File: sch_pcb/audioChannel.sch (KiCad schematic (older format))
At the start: 87 parts, among them J201 TO_SOUNDCARD, J202 FROM_SOUNDCARD, J203 Radio Port, J404 DB9_FEMALE, Q201 2N7000, Q202 2N7000, Q203 2N7000, U103 MCP4351, U106 MCP4351, U201 MCP6004N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

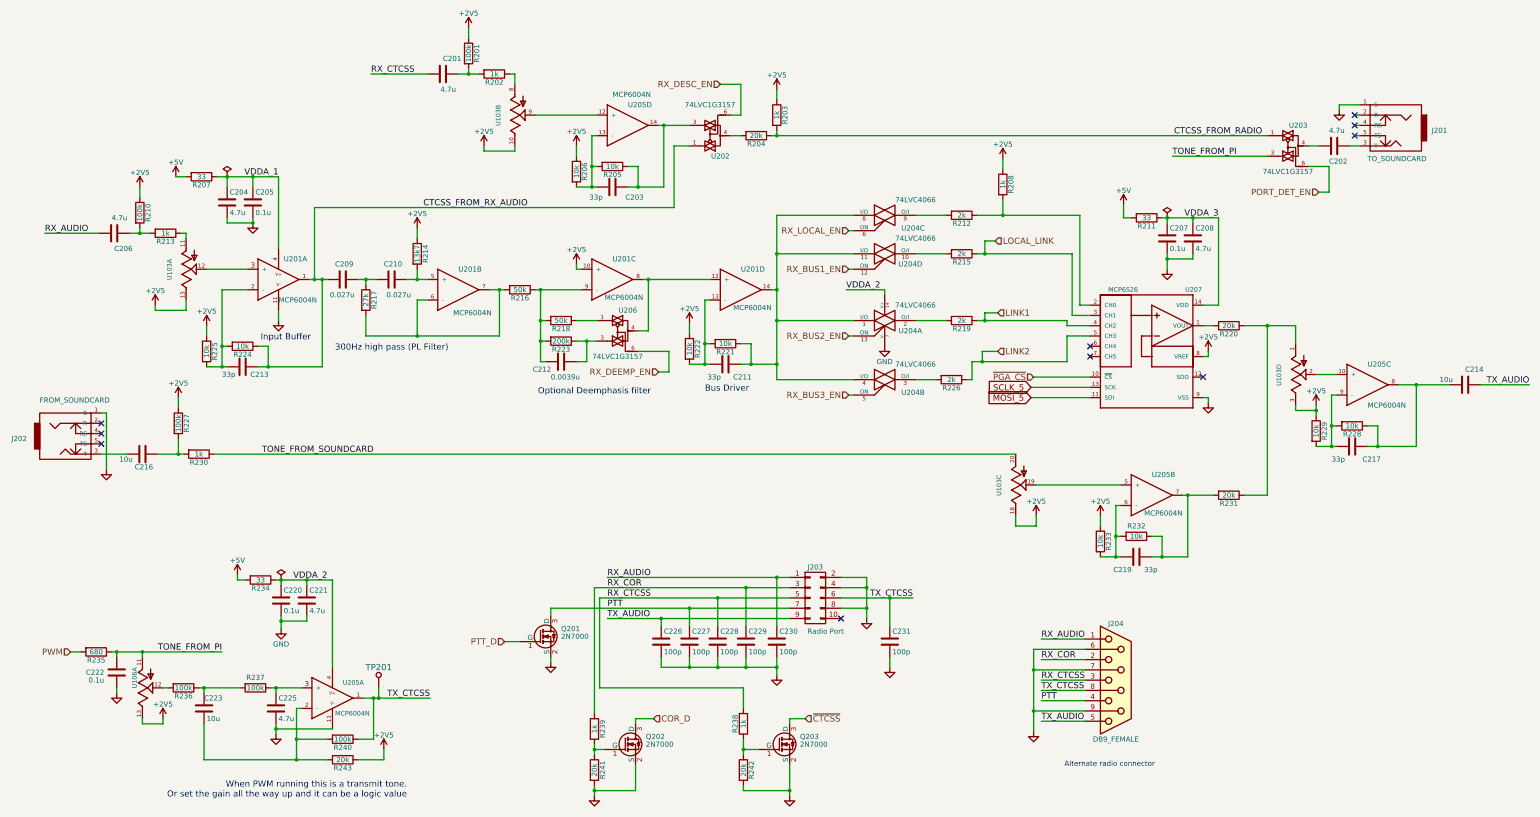
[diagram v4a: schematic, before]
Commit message: Add files via upload
Change link connectors to use a daughterboard for the off-rack links and 100mil headers for between-board links
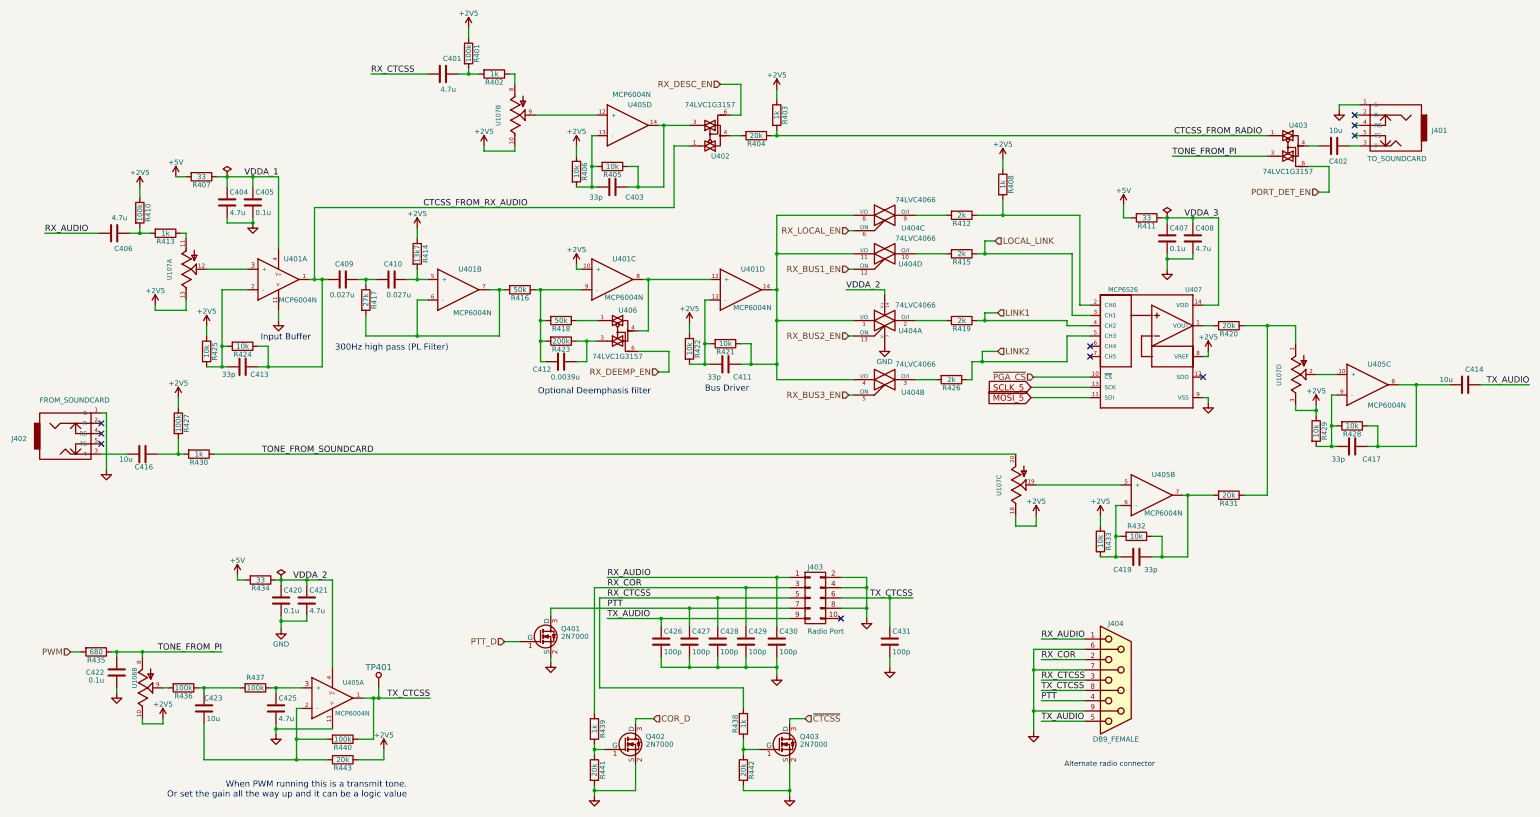
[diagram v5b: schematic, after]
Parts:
- C202: value 4.7u -> 10u
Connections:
- net +2V5: now also U106.10 (B); no longer U106.13 (B)
- net TONE_FROM_PI: now also U106.8 (A); no longer U106.11 (A)
- net at R236.2: now also U106.9 (W); no longer U106.12 (W)

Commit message: Add soundcard schematic
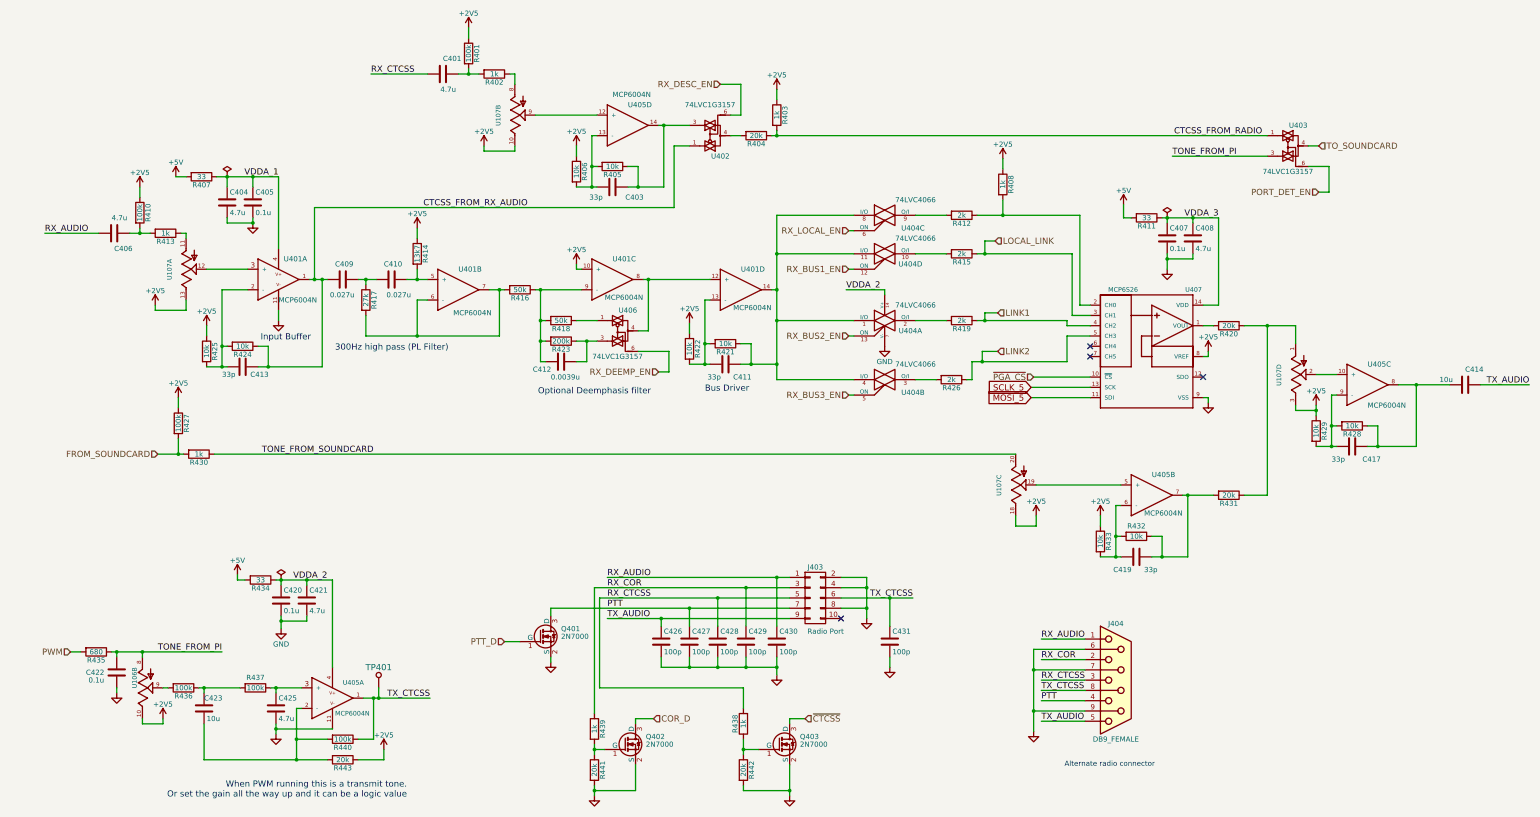
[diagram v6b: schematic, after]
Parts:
- removed C202: 10u, lib:smd0603, symbol C
- removed C216: 10u, lib:smd0805, symbol C
- removed J201: TO_SOUNDCARD, lib:TRS3.5_5, symbol JACK_TRS
- removed J202: FROM_SOUNDCARD, lib:TRS3.5_5, symbol JACK_TRS
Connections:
- net TO_SOUNDCARD: now reaches U203.4
- net FROM_SOUNDCARD: now reaches R227.2, R230.2
- no-connect marks 10 -> 4

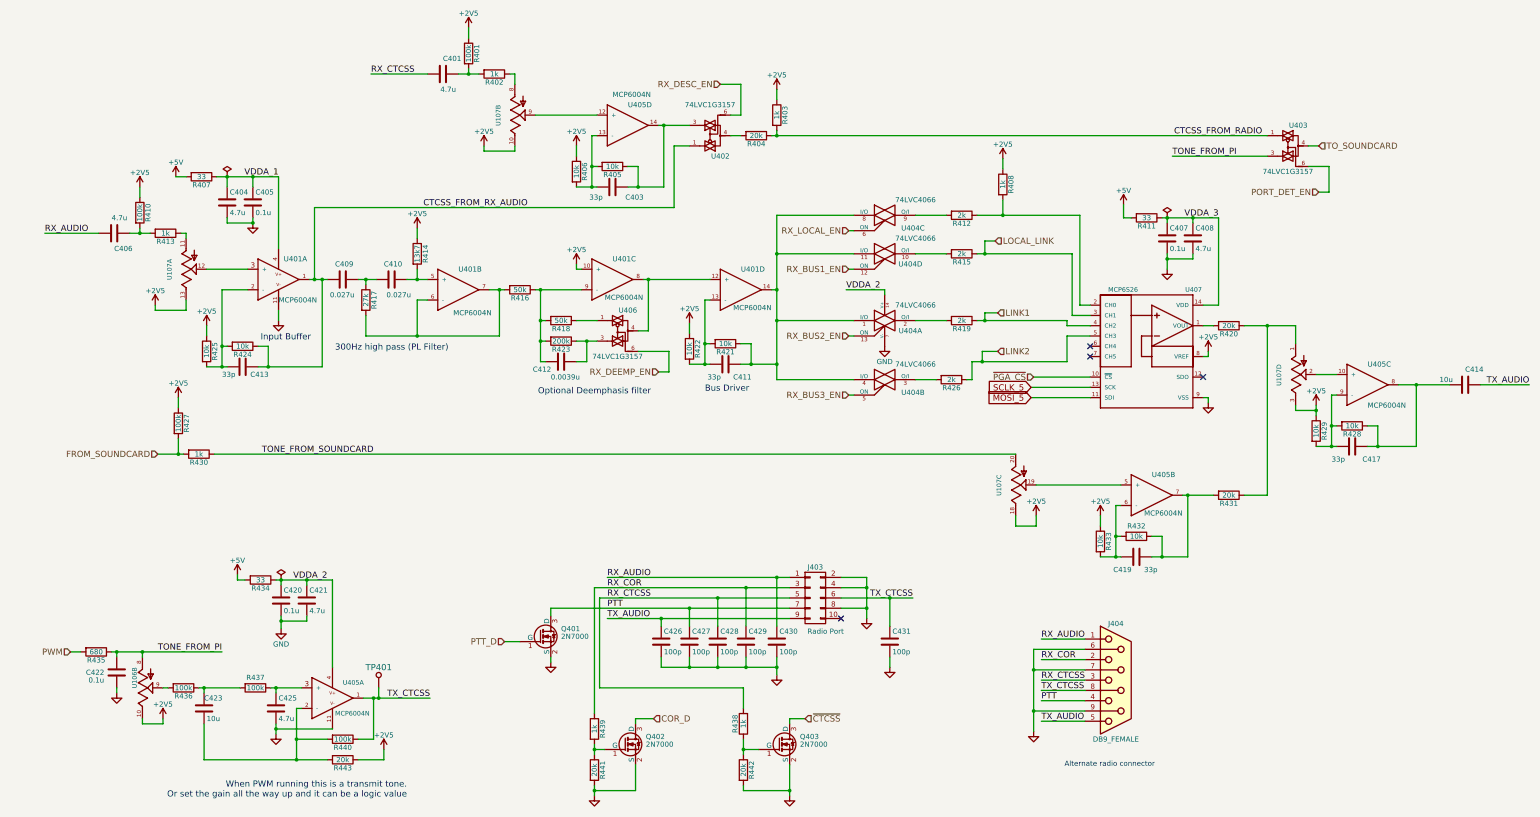
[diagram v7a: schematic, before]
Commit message: Update from latest round of emails
Change connectors - use correct footprint for DE9F.  Add chassis connector as DE9M, AUX_IO connectors as 116-pin ribbon, expected to transition to DA15 with a cable.  
Remove screw terminals for 12V input as it now comes in on chassis connector
Remove third EEPOT package
Move stuff off PCB in preparation to incorporate all the schematic updates.
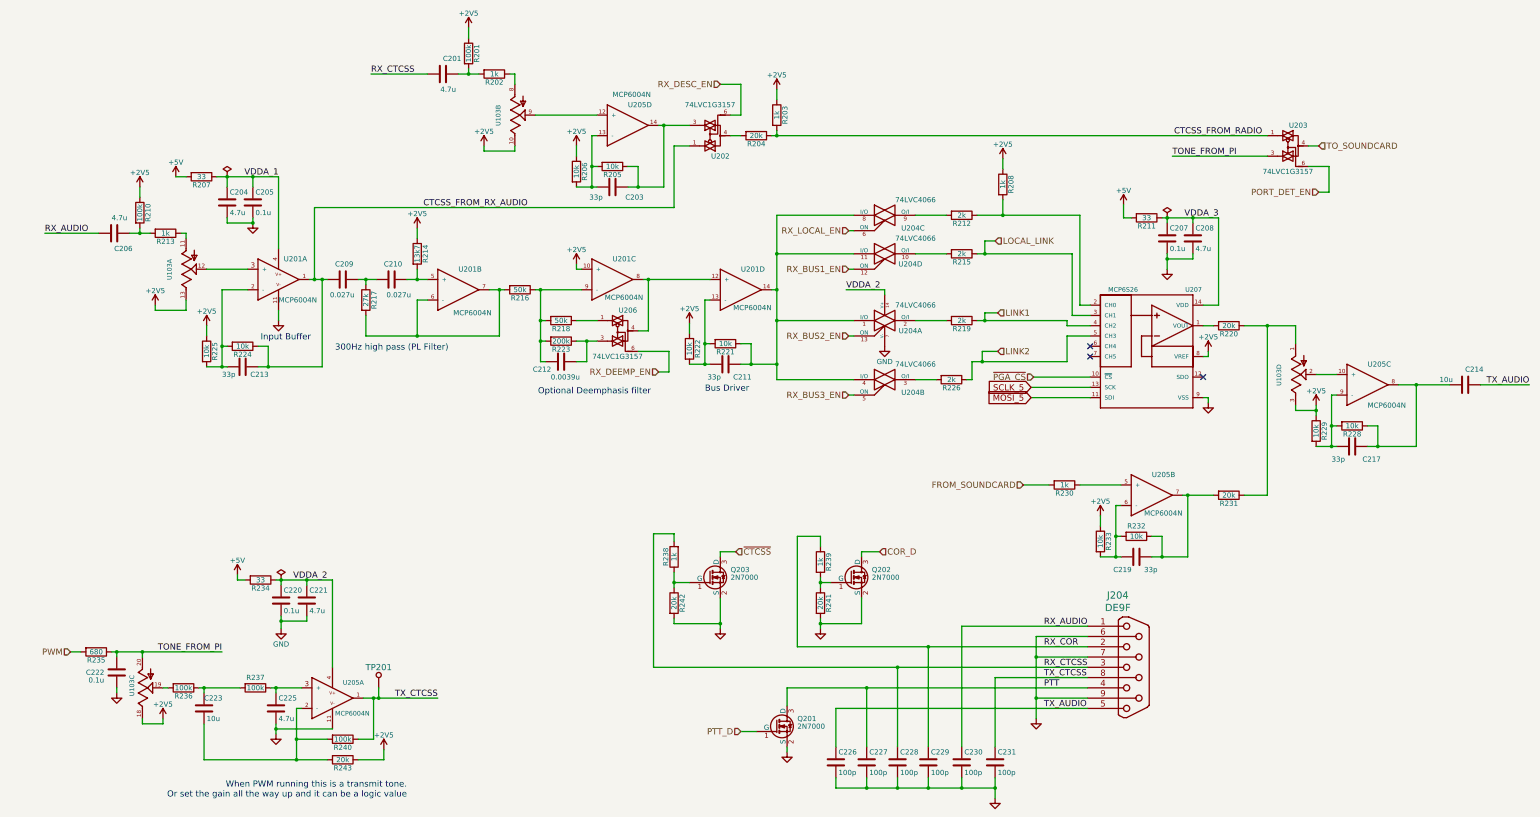
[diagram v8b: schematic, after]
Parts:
- removed J203: Radio Port, lib:RibbonHeader2x5, symbol CONN_02X05
- removed J404: DB9_FEMALE, lib:DB9FC, symbol DB9_FEMALE
- removed R227: 100k, lib:smd0603, symbol R
- removed unit 3 of U103
- added J204: DE9F, lib:DE9F_Right_Angle, symbol DE9
- renumbered U106 to U103
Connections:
- net TONE_FROM_SOUNDCARD is gone; now on an unnamed net: R230.1
- net +2V5: now also U103.18 (B); no longer U103.10 (B)
- net GND: now also J204.6 (P6), J204.7 (P7), J204.9 (P9)
- net PTT: now also J204.4
- net RX_AUDIO: now also J204.1
- net RX_COR: now also J204.2
- net RX_CTCSS: now also J204.3
- net TONE_FROM_PI: now also U103.20 (A); no longer U103.8 (A)
- net TX_AUDIO: now also J204.5
- net TX_CTCSS: now also J204.8 (P8)
- net at R236.2: now also U103.19 (W); no longer U103.9 (W)
- no-connect marks 4 -> 3
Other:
- note removed: "Alternate radio connector"
- moved on the sheet: C226, C227, C228, C229, C230, C231, Q201, Q202, Q203, R230, R238, R239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
